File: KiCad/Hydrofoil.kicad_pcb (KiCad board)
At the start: 2 copper layers, 219.6 x 35 mm, 65 parts, among them J1 Conn_01x03_Pin, J2 Conn_01x03_Pin, Q1 AO3413, Q2 BSS138, Q3 BSS138, Q4 BSS138, Q5 BSS138, Q6 BSS138, U1 LD1117S33CTR, U2 ESP32-C3-MINI-1-N4, U3 ADS1115IDGS, U4 LM334M, U5 LM334M, U6 LM334M

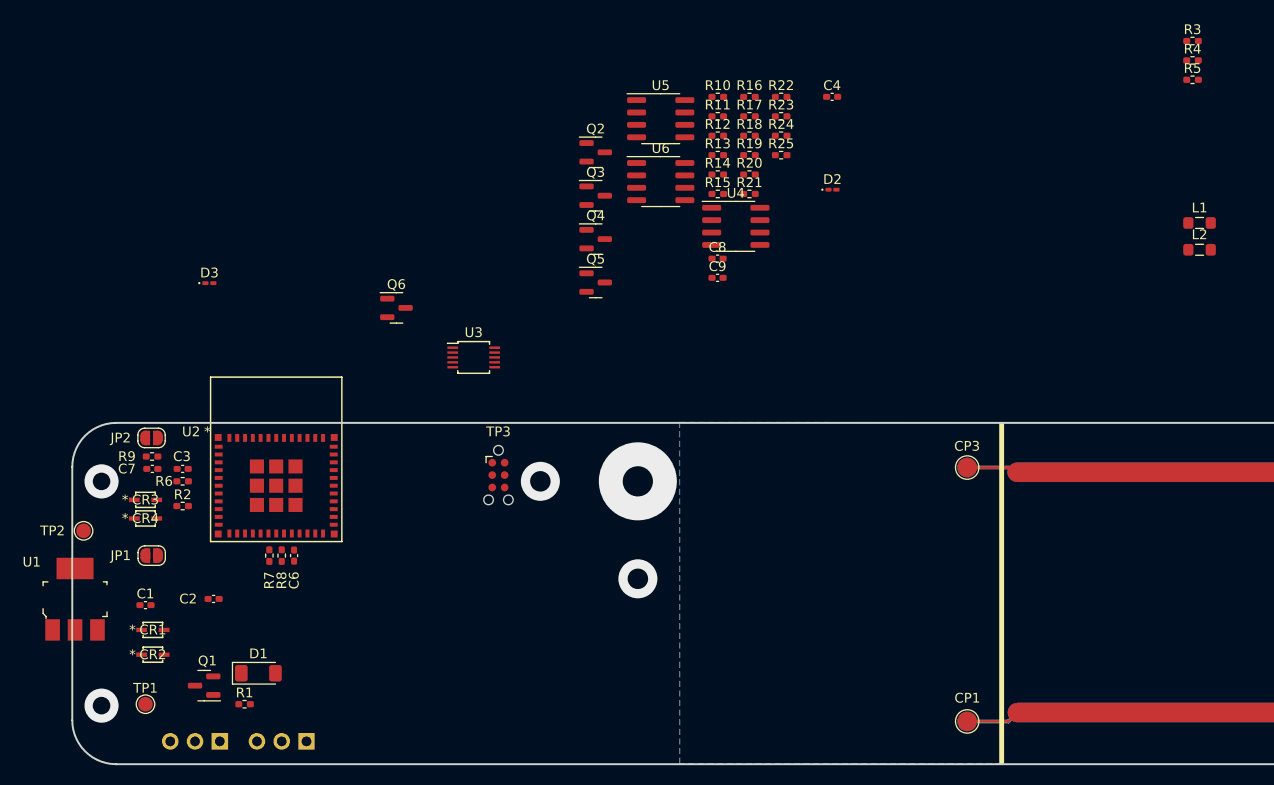
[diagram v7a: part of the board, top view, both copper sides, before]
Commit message: Organize parts on the PCB
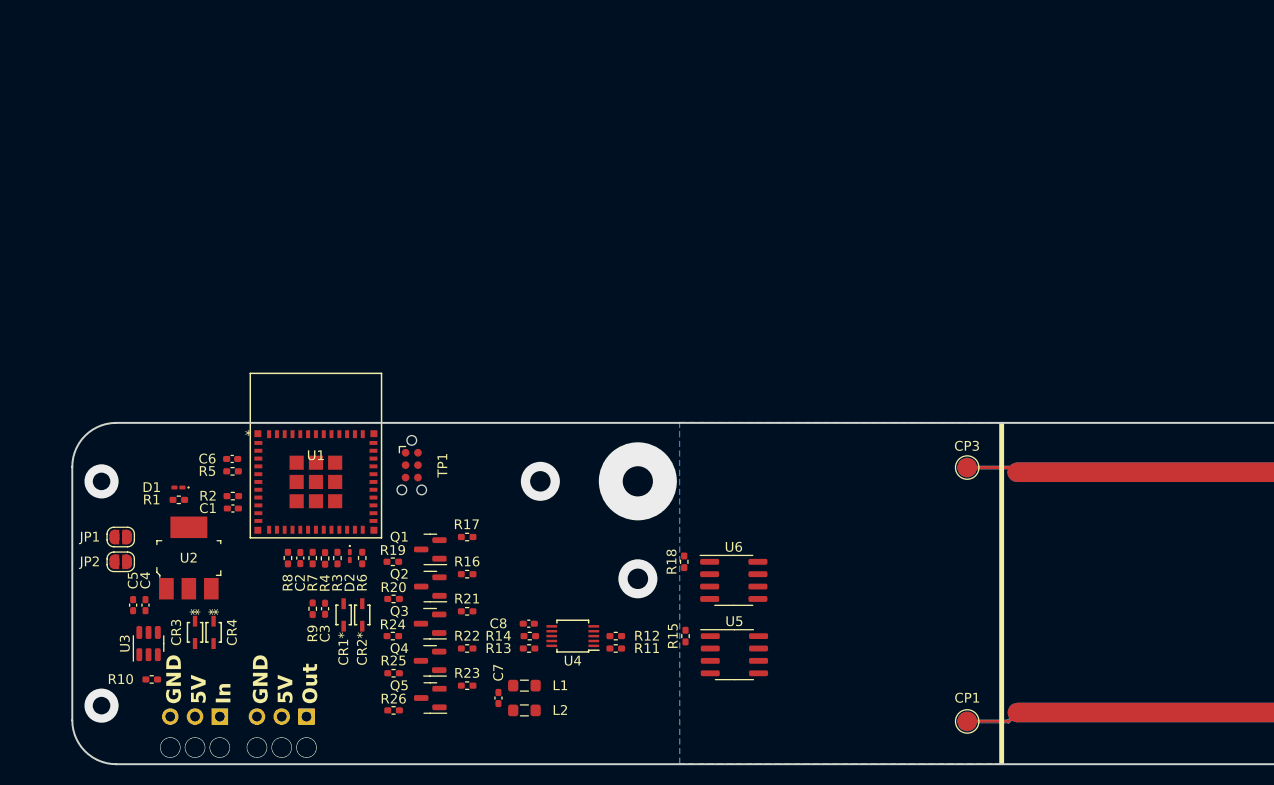
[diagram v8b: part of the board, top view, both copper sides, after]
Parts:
- removed C9: 1u, Capacitor_SMD:C_0402_1005Metric_Pad0.74x0.62mm_HandSolder
- removed D3: Red, LED_SMD:LED_0201_0603Metric_Pad0.64x0.40mm_HandSolder
- removed Q6: BSS138, Package_TO_SOT_SMD:SOT-23
- removed TP2: TestPoint, TestPoint:TestPoint_Pad_D1.5mm
- removed TP3: ~, Connector:Tag-Connect_TC2030-IDC-NL_2x03_P1.27mm_Vertical
- added C5: 10u, Capacitor_SMD:C_0402_1005Metric_Pad0.74x0.62mm_HandSolder, F.Cu at (45.1, 89.5)
- added R26: 10k, Resistor_SMD:R_0402_1005Metric_Pad0.72x0.64mm_HandSolder, F.Cu at (71.8, 100.3)
- C1, C2, C3: value 10u -> 1u
- C4, C6: value 1u -> 10u
- D1: value BZV55B7V5 -> Green; footprint Diode_SMD:D_MiniMELF -> LED_SMD:LED_0201_0603Metric_Pad0.64x0.40mm_HandSolder
- D2: value Green -> Red
- JP1: value Jumper_2_Open -> Reset Settings
- JP2: value Jumper_2_Open -> Boot
- Q1: value AO3413 -> BSS138
- R1: value 100k -> 1k
- R14, R17: value 150R -> 10k
- R15, R18: value 10k -> 150R
- R3: value 1k -> 10k
- TP1: value TestPoint -> ~; footprint TestPoint:TestPoint_Pad_D1.5mm -> Connector:Tag-Connect_TC2030-IDC-NL_2x03_P1.27mm_Vertical
- U1: value LD1117S33CTR -> ESP32-C3-MINI-1-N4; footprint digikey-footprints:SOT-223 -> ESP32-C3-MINI-1-N4:ESP32-C3-MINI-1_EXP
- U2: value ESP32-C3-MINI-1-N4 -> LD1117S33CTR; footprint ESP32-C3-MINI-1-N4:ESP32-C3-MINI-1_EXP -> digikey-footprints:SOT-223
- U3: value ADS1115IDGS -> TPS22917DBV; footprint Package_SO:TSSOP-10_3x3mm_P0.5mm -> Package_TO_SOT_SMD:SOT-23-6
- U4: value LM334M -> ADS1115IDGS; footprint Package_SO:SOIC-8_3.9x4.9mm_P1.27mm -> Package_SO:TSSOP-10_3x3mm_P0.5mm
- moved R5 106.3 mm to (55.3, 75.8)
- moved R4 102.6 mm to (64.8, 84.7), turned to 90 degrees
- moved R3 102.5 mm to (66.0, 84.7), turned to 90 degrees
- moved C4 87.6 mm to (46.4, 89.5), turned to 90 degrees
- moved L1 83.9 mm to (85.2, 97.8), turned to 180 degrees
- moved L2 83.8 mm to (85.2, 100.3), turned to 180 degrees
- moved R10 83.3 mm to (47.0, 97.2), turned to 180 degrees
- moved R23 66.7 mm to (79.3, 97.8), turned to 180 degrees
- moved R25 66.3 mm to (71.8, 96.5)
- moved R22 65.1 mm to (79.3, 94.0), turned to 180 degrees
- moved R24 64.9 mm to (71.7, 92.7)
- moved D2 62.1 mm to (67.3, 84.5), turned to -90 degrees
- moved R16 56.9 mm to (79.3, 86.4), turned to 180 degrees
- moved R20 56.8 mm to (71.8, 88.9)
- moved R11 55.6 mm to (94.6, 94.0)
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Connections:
- C1 pad 1: /+5V-Logic -> ESP-En
- C2 pad 1: +5V -> Input-Reset
- C3 pad 1: +3.3V -> Net-(C3-Pad1)
- C4 pad 1: Net-(U2-EN) -> /+5V-Logic
- C6 pad 1: Input-Reset -> +3.3V
- C7 pad 1: Net-(C7-Pad1) -> +5V
- C8 pad 1: +5V -> GNDA
- C8 pad 2: GND -> +5VA
- CR1 pad 1: /+5V-Logic -> Net-(C3-Pad1)
- CR1 pad 2: +5V -> Input-Boot
- CR2 pad 1: /+5V-Logic -> ESP-Boot
- CR2 pad 2: +5V-Prog -> Input-Boot
- CR3 pad 1: Net-(C7-Pad1) -> /+5V-Logic
- CR3 pad 2: Input-Boot -> +5V
- CR4 pad 1: ESP-Boot -> /+5V-Logic
- CR4 pad 2: Input-Boot -> +5V-Prog
- D1 pad 1: +5V -> GND
- D2 pad 1: GND -> User-LED
- Q1 pad 1: Net-(D1-A) -> +3.3V
- Q1 pad 2: +5V -> Ready-LV
- Q1 pad 3: /+5V-Raw -> Ready-HV
- Q2 pad 2: Ready-LV -> SDA-LV
- Q2 pad 3: Ready-HV -> SDA-HV
- Q3 pad 2: SDA-LV -> SCL-LV
- Q3 pad 3: SDA-HV -> SCL-HV
- Q4 pad 2: SCL-LV -> PWM-In-LV
- Q4 pad 3: SCL-HV -> PWM-In-HV
- Q5 pad 2: PWM-In-LV -> PWM-Out-LV
- Q5 pad 3: PWM-In-HV -> PWM-Out-HV
- R1 pad 1: Net-(D1-A) -> +3.3V
- R1 pad 2: GND -> Net-(D1-A)
- R10 pad 1: Net-(U3-ADDR) -> Net-(U3-ON)
- R10 pad 2: GNDA -> /+5V-Raw
- R11 pad 1: +5VA -> Net-(U4-ADDR)
- R11 pad 2: Ready-HV -> GNDA
- R12 pad 2: SCL-HV -> Ready-HV
- R13 pad 2: SDA-HV -> SCL-HV
- R14 pad 1: /ADS1115-ADC/SETcur1 -> +5VA
- R14 pad 2: AIN0 -> SDA-HV
- R15 pad 1: unconnected-(R15-Pad1) -> /ADS1115-ADC/SETcur1
- R15 pad 2: unconnected-(R15-Pad2) -> AIN0
- R16 pad 2: Ready-LV -> SDA-LV
- R17 pad 1: /ADS1115-ADC/SETcur2 -> +3.3V
- R17 pad 2: AIN1 -> Ready-LV
- R18 pad 1: +5VA -> /ADS1115-ADC/SETcur2
- R18 pad 2: Ready-HV -> AIN1
- R19 pad 2: SDA-HV -> Ready-HV
- R2 pad 2: Net-(U2-EN) -> ESP-En
- R20 pad 1: +3.3V -> +5VA
- R20 pad 2: SCL-LV -> SDA-HV
- R21 pad 2: PWM-In-LV -> SCL-LV
- R22 pad 2: PWM-Out-LV -> PWM-In-LV
- R23 pad 1: +5VA -> +3.3V
- R23 pad 2: SCL-HV -> PWM-Out-LV
- R24 pad 2: PWM-In-HV -> SCL-HV
- R25 pad 2: PWM-Out-HV -> PWM-In-HV
- R3 pad 2: Net-(D2-A) -> User-LED
- R4 pad 2: Net-(D3-A) -> Net-(D2-A)
- R5 pad 2: User-LED -> Net-(U1-IO2)
- R9 pad 1: Net-(C7-Pad1) -> Net-(C3-Pad1)
- TP1 pad 1: +5V -> ESP-En
- U1 pad 2: +3.3V -> GND
- U1 pad 3: /+5V-Logic -> +3.3V
- U1 pad 4: +3.3V -> unconnected-(U1-NC-Pad4)
- U2 pad 2: GND -> +3.3V
- U2 pad 3: +3.3V -> /+5V-Logic
- U2 pad 4: unconnected-(U2-NC-Pad4) -> +3.3V
- U3 pad 1: Net-(U3-ADDR) -> /+5V-Raw
- U3 pad 2: Ready-HV -> GND
- U3 pad 3: GNDA -> Net-(U3-ON)
- U3 pad 4: AIN0 -> unconnected-(U3-CT-Pad4)
- U3 pad 5: AIN1 -> unconnected-(U3-QOD-Pad5)
- U3 pad 6: unconnected-(U3-AIN2-Pad6) -> +5V
- U4 pad 1: /ADS1115-ADC/SETcur1 -> Net-(U4-ADDR)
- U4 pad 2: AIN0 -> Ready-HV
- U4 pad 3: AIN0 -> GNDA
- U4 pad 4: +5VA -> AIN0
- U4 pad 5: (no net) -> AIN1
- U4 pad 6: AIN0 -> unconnected-(U4-AIN2-Pad6)
- U4 pad 7: AIN0 -> unconnected-(U4-AIN3-Pad7)
- U4 pad 8: (no net) -> +5VA
- U5 pad 1: /ADS1115-ADC/SETcur2 -> /ADS1115-ADC/SETcur1
- U5 pad 2: AIN1 -> AIN0
- U5 pad 3: AIN1 -> AIN0
- U5 pad 6: AIN1 -> AIN0
- U5 pad 7: AIN1 -> AIN0
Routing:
- net (no net): vias 5 -> 11
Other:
- board text added: "5V"
- board text added: "GND"
- board text added: "In"
- board text added: "Out"
